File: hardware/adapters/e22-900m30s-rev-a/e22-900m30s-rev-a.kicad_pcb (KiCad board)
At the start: 2 copper layers, 84 x 80 mm, 27 parts, among them J1 TSW-110-07-G-S, J2 TSW-108-07-G-S, U1 E22-900M30S

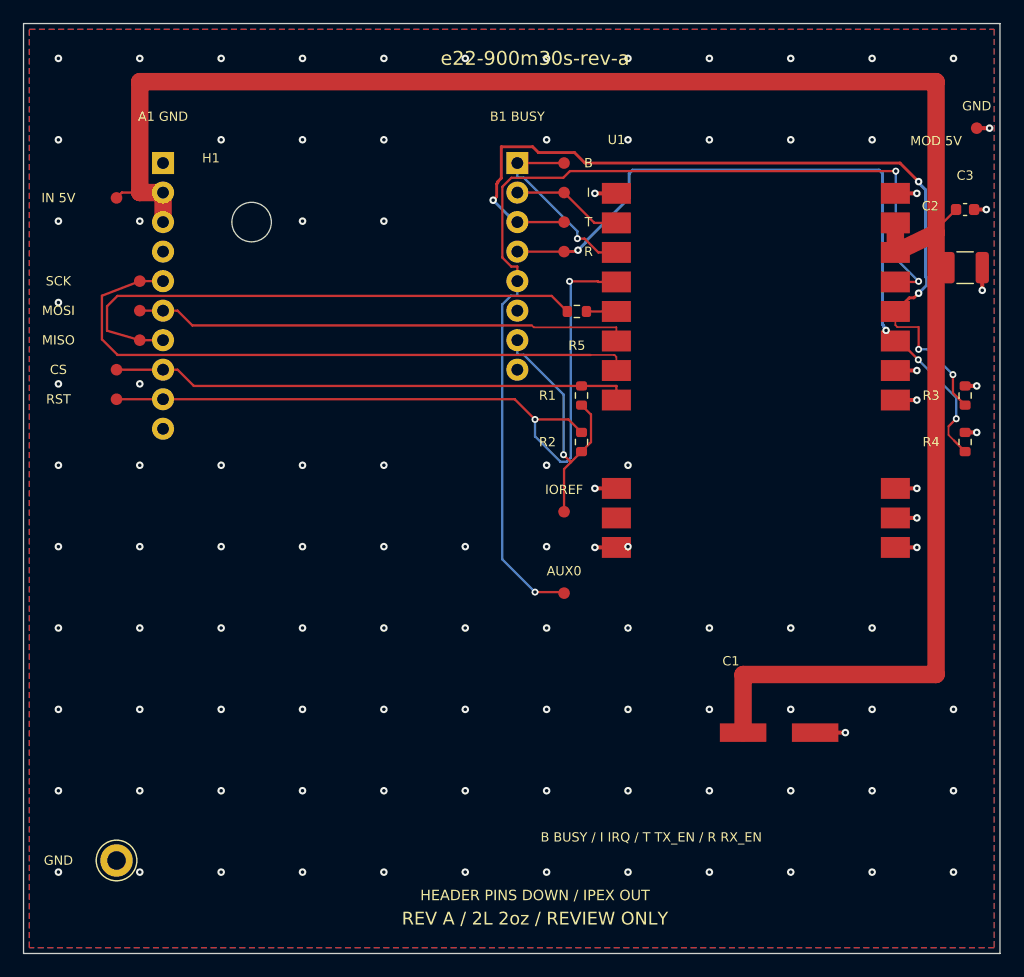
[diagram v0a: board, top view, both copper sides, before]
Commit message: Improve Rev-A ground references and feedback routing
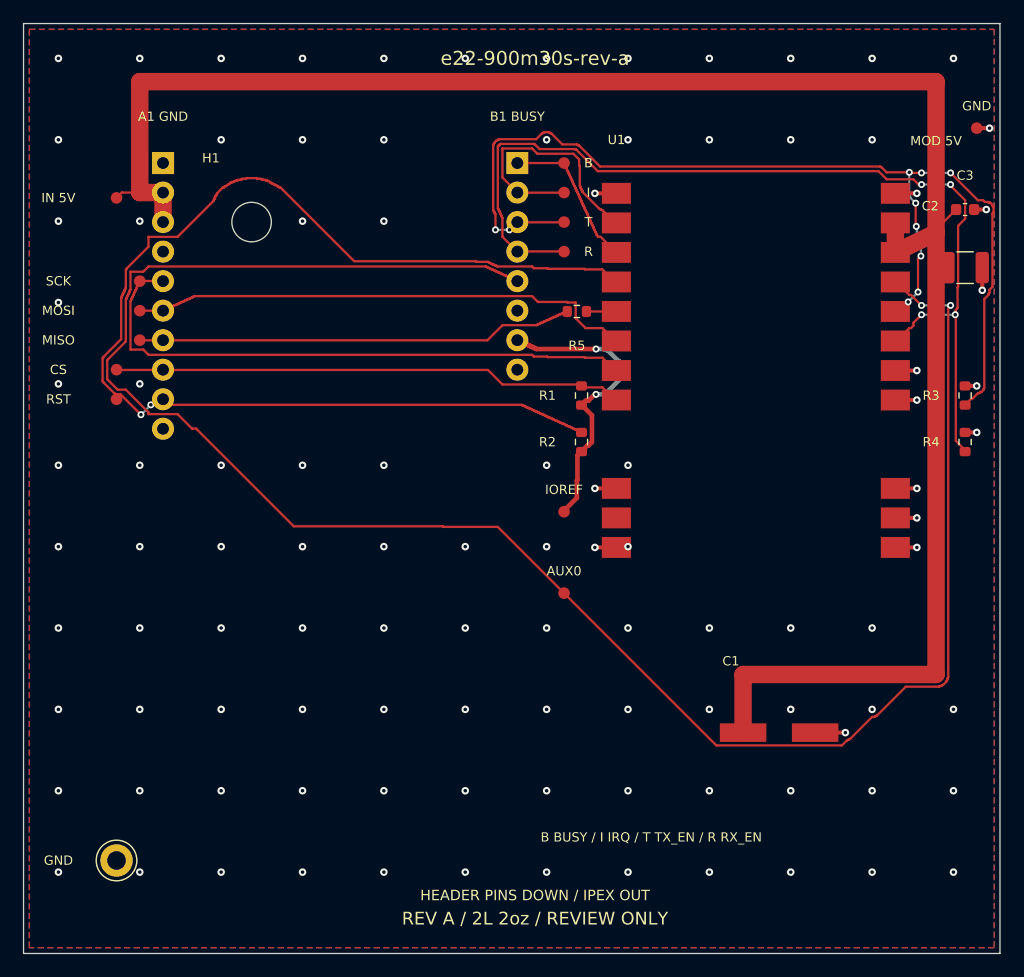
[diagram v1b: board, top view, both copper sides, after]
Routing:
- net /AUX0: track 87.0 -> 169.8 mm, vias 3 -> 2
- net /RESET_N: track 66.0 -> 105.0 mm
- net /RX_EN: track 63.4 -> 84.7 mm
- net /TX_EN: track 74.5 -> 91.5 mm, vias 5 -> 10
- net /IRQ: track 9.60 -> 22.3 mm
- net /SPI_MISO: track 47.5 -> 37.8 mm
- net /SPI_SCK: track 55.3 -> 50.8 mm
- net /IOREF_3V3: track 23.2 -> 26.4 mm, vias 1 -> 2
- net /BUSY: track 16.8 -> 13.7 mm, vias 1 -> 0
- net /SPI_MOSI: track 42.8 -> 43.9 mm
- net /CS_N: track 44.8 -> 44.1 mm
